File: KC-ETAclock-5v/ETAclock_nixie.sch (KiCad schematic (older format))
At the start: 91 parts, among them Q10 MMBTA42, Q11 MMBTA92, Q12 MMBTA42, Q13 MMBTA92, Q14 MMBTA42, Q15 MMBTA92, Q16 MMBTA42, Q17 MMBTA92, Q18 MMBTA42, Q19 MMBTA92, Q2 MMBTA42, Q20 MMBTA42, Q21 MMBTA92, Q22 MMBTA42, Q23 MMBTA92, Q24 MMBTA42, Q25 MMBTA92, Q3 MMBTA92, Q4 MMBTA42, Q5 MMBTA92, Q6 MMBTA42, Q7 MMBTA92, Q8 MMBTA42, Q9 MMBTA92, U10 IN-4, U11 TPIC6B595, U12 IN-4, U13 IN-4, U14 TPIC6B595, U3 IN-4, U4 TPIC6B595, U5 IN-4, U6 74HCT04, U7 TPIC6B595, U8 IN-4, U9 TPIC6B595

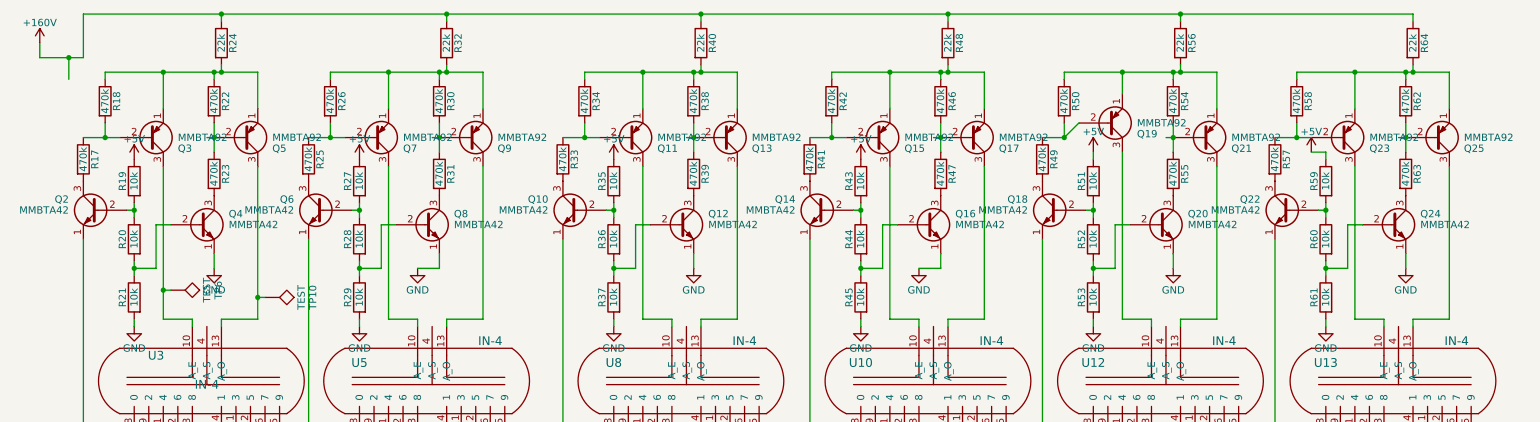
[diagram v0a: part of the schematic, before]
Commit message: New Layout changes.  Fixed the BJT packages.  Added 1k to the 160v_enable pin to protect the rasberry pi.  Improved the 160v spacing to the power supply input.
updated the code with both a testscript and a testETAclock.py to help test the code.
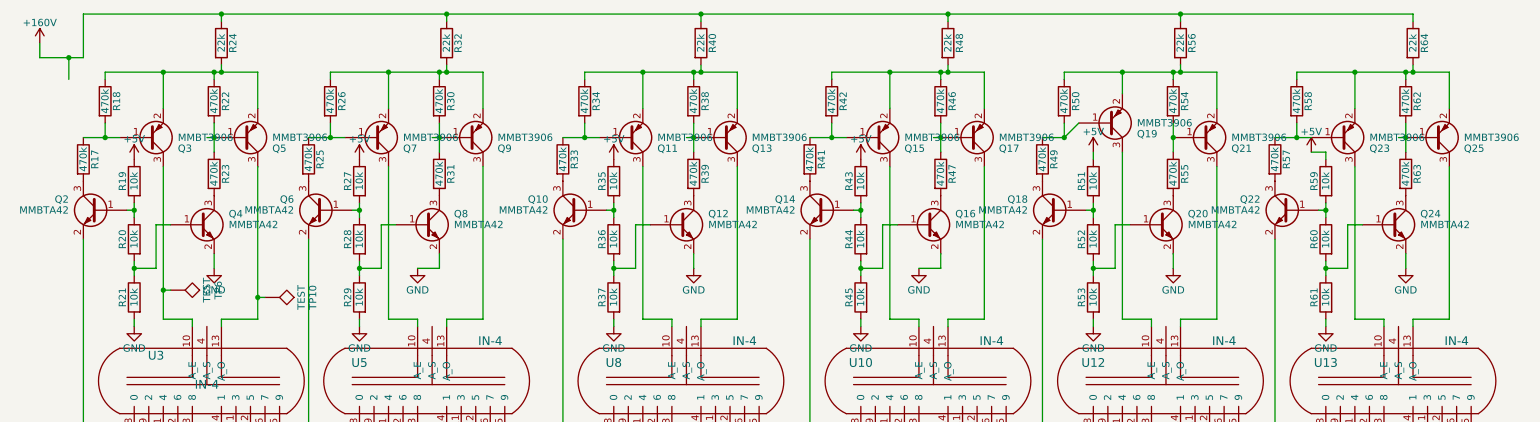
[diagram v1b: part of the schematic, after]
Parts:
- removed Q10, Q12, Q14, Q16, Q18, Q2, Q20, Q22, Q24, Q4, Q6, Q8: MMBTA42, TO_SOT_Packages_SMD:SOT-23, symbol MPSA42
- removed Q11, Q13, Q15, Q17, Q19, Q21, Q23, Q25, Q3, Q5, Q7, Q9: MMBTA92, TO_SOT_Packages_SMD:SOT-23, symbol MPSA92
- added Q10, Q12, Q14, Q16, Q18, Q2, Q20, Q22, Q24, Q4, Q6, Q8: MMBTA42, TO_SOT_Packages_SMD:SOT-23, symbol MMBT3904
- added Q11, Q13, Q15, Q17, Q19, Q21, Q23, Q25, Q3, Q5, Q7, Q9: MMBT3906, TO_SOT_Packages_SMD:SOT-23, symbol MMBT3906
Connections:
- net GND: now also Q12.2 (E), Q16.2 (E), Q20.2 (E), Q24.2 (E), Q4.2 (E), Q8.2 (E)
- net at TP6.1, U3.10 (A_E): now also Q3.3 (C)
- net at TP10.1, U3.13 (A_O): now also Q5.3 (C)
- net at U5.10 (A_E): now also Q7.3 (C)
- net at U5.13 (A_O): now also Q9.3 (C)
- net at U8.10 (A_E): now also Q11.3 (C)
- net at U8.13 (A_O): now also Q13.3 (C)
- net at U10.10 (A_E): now also Q15.3 (C)
- net at U10.13 (A_O): now also Q17.3 (C)
- net at U12.10 (A_E): now also Q19.3 (C)
- net at U12.13 (A_O): now also Q21.3 (C)
- net at U13.10 (A_E): now also Q23.3 (C)
- net at U13.13 (A_O): now also Q25.3 (C)
- net at R18.1, R22.1, R24.2: now also Q3.2 (E), Q5.2 (E)
- net at R17.1, R18.2: now also Q3.1 (B)
- net at R17.2: now also Q2.3 (C)
- net at R22.2, R23.1: now also Q5.1 (B)
- net at R23.2: now also Q4.3 (C)
- net at R19.2, R20.1: now also Q2.1 (B)
- net at R20.2, R21.1: now also Q4.1 (B)
- net at R26.1, R30.1, R32.2: now also Q7.2 (E), Q9.2 (E)
- net at R25.1, R26.2: now also Q7.1 (B)
- net at R25.2: now also Q6.3 (C)
- net at R30.2, R31.1: now also Q9.1 (B)
- net at R31.2: now also Q8.3 (C)
- net at R27.2, R28.1: now also Q6.1 (B)
- net at R28.2, R29.1: now also Q8.1 (B)
- net at R34.1, R38.1, R40.2: now also Q11.2 (E), Q13.2 (E)
- net at R33.1, R34.2: now also Q11.1 (B)
- net at R33.2: now also Q10.3 (C)
- net at R38.2, R39.1: now also Q13.1 (B)
- net at R39.2: now also Q12.3 (C)
- net at R35.2, R36.1: now also Q10.1 (B)
- net at R36.2, R37.1: now also Q12.1 (B)
- net at R42.1, R46.1, R48.2: now also Q15.2 (E), Q17.2 (E)
- net at R41.1, R42.2: now also Q15.1 (B)
- net at R41.2: now also Q14.3 (C)
- net at R46.2, R47.1: now also Q17.1 (B)
- net at R47.2: now also Q16.3 (C)
- net at R43.2, R44.1: now also Q14.1 (B)
- net at R44.2, R45.1: now also Q16.1 (B)
- net at R50.1, R54.1, R56.2: now also Q19.2 (E), Q21.2 (E)
- net at R49.1, R50.2: now also Q19.1 (B)
- net at R49.2: now also Q18.3 (C)
- net at R54.2, R55.1: now also Q21.1 (B)
- net at R55.2: now also Q20.3 (C)
- net at R51.2, R52.1: now also Q18.1 (B)
- net at R52.2, R53.1: now also Q20.1 (B)
- net at R58.1, R62.1, R64.2: now also Q23.2 (E), Q25.2 (E)
- net at R57.1, R58.2: now also Q23.1 (B)
- net at R57.2: now also Q22.3 (C)
- net at R62.2, R63.1: now also Q25.1 (B)
- net at R63.2: now also Q24.3 (C)
- net at R59.2, R60.1: now also Q22.1 (B)
- net at R60.2, R61.1: now also Q24.1 (B)
- net at U11.16 (D6): now also Q22.2 (E)
- net at U11.4 (D0): now also Q18.2 (E)
- net at U9.6 (D2): now also Q14.2 (E)
- net at U7.14 (D4): now also Q10.2 (E)
- net at U4.16 (D6): now also Q6.2 (E)
- net at U4.4 (D0): now also Q2.2 (E)

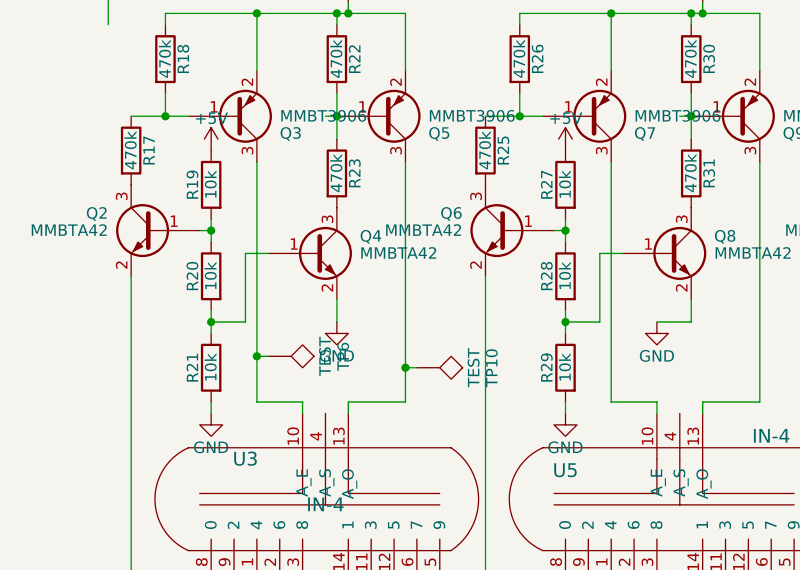
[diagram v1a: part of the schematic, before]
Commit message: The TestDigits.py is a script file that allows for the following feastures:
- cycle through all digits 1 second at a time
- display any single digit
- burn in all digits
- burn in even digits
- burn in odd digits
- toggle N_DISABLE
- toggle POWER

here is the command from the python script.

 print("press:")
   print("return: to index the displayed diget to the next value")
   print("[t]: to start time 1-9:")
   print("[T]: For a x minute burn in of all digits")
   print("[0-9]: to display the digit to light up")
   print("[d]: to toggle display N_DISABLE")
   print("[p]: to toggle the power supply on/off")
   print("[OT]: for a x minute burn in of odd digits (for biquaniary driven tubes")
   print("[ET]: for a x minute burn in of even digits (for biquinary driven tubes)")
   print("[x]: to exit program")
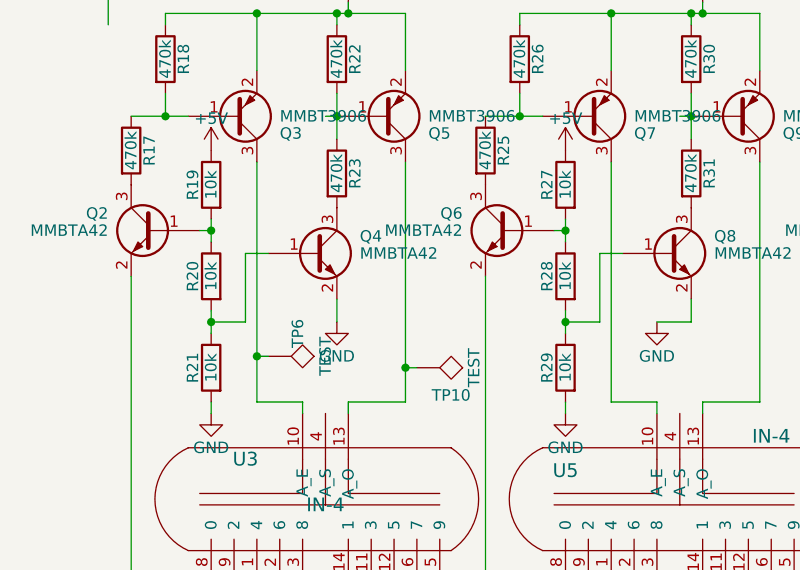
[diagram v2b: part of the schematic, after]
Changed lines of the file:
@@
 	2000 2750 2000 2700
 Wire Wire Line
-	2250 2700 2000 2700
-Wire Wire Line
-	2250 1650 2250 2700
+	2000 2700 2250 2700
+Wire Wire Line
+	2250 2700 2250 1650
 Wire Wire Line
 	2250 1000 2250 1250
@@
 U 1 1 5A933969
 P 1650 2500
-F 0 "TP6" H 1650 2800 50  0000 C BNN
+F 0 "TP6" H 1550 2600 50  0000 C BNN
 F 1 "TEST" H 1650 2750 50  0000 C CNN
 F 2 "Connectors:PINTST" H 1650 2500 50  0001 C CNN
@@
 U 1 1 5A933F4D
 P 2300 2550
-F 0 "TP10" H 2300 2850 50  0000 C BNN
+F 0 "TP10" V 2450 2700 50  0000 C BNN
 F 1 "TEST" H 2300 2800 50  0000 C CNN
 F 2 "Connectors:PINTST" H 2300 2550 50  0001 C CNN
